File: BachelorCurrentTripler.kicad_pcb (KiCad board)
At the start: 2 copper layers, 54 parts, among them Q13 C2M0025120D, Q14 C2M0025120D, Q15 C2M0025120D, Q16 C2M0025120D, Q7 C2M0025120D, Q8 C2M0025120D, U1 STDriveG600, U2 STDriveG600, U3 STDriveG600

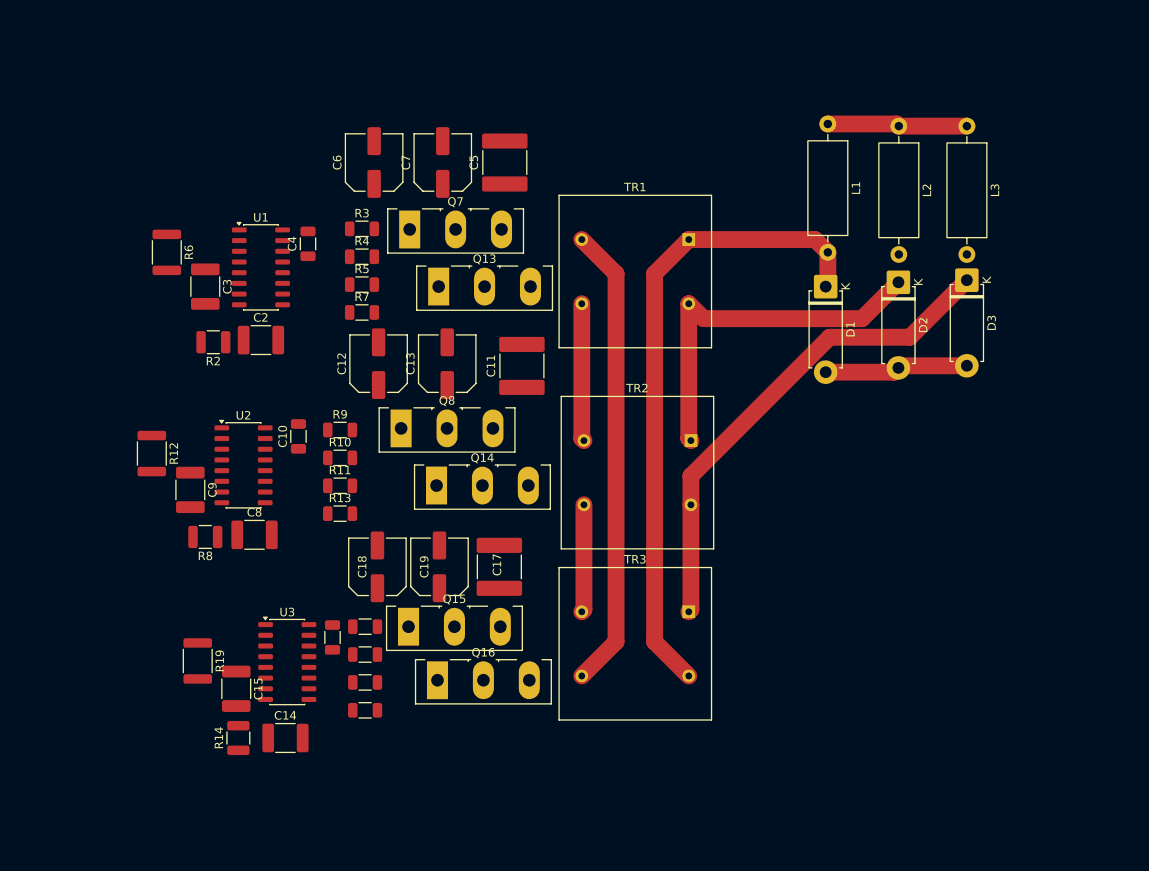
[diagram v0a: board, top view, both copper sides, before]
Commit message: added a board outline and some holes
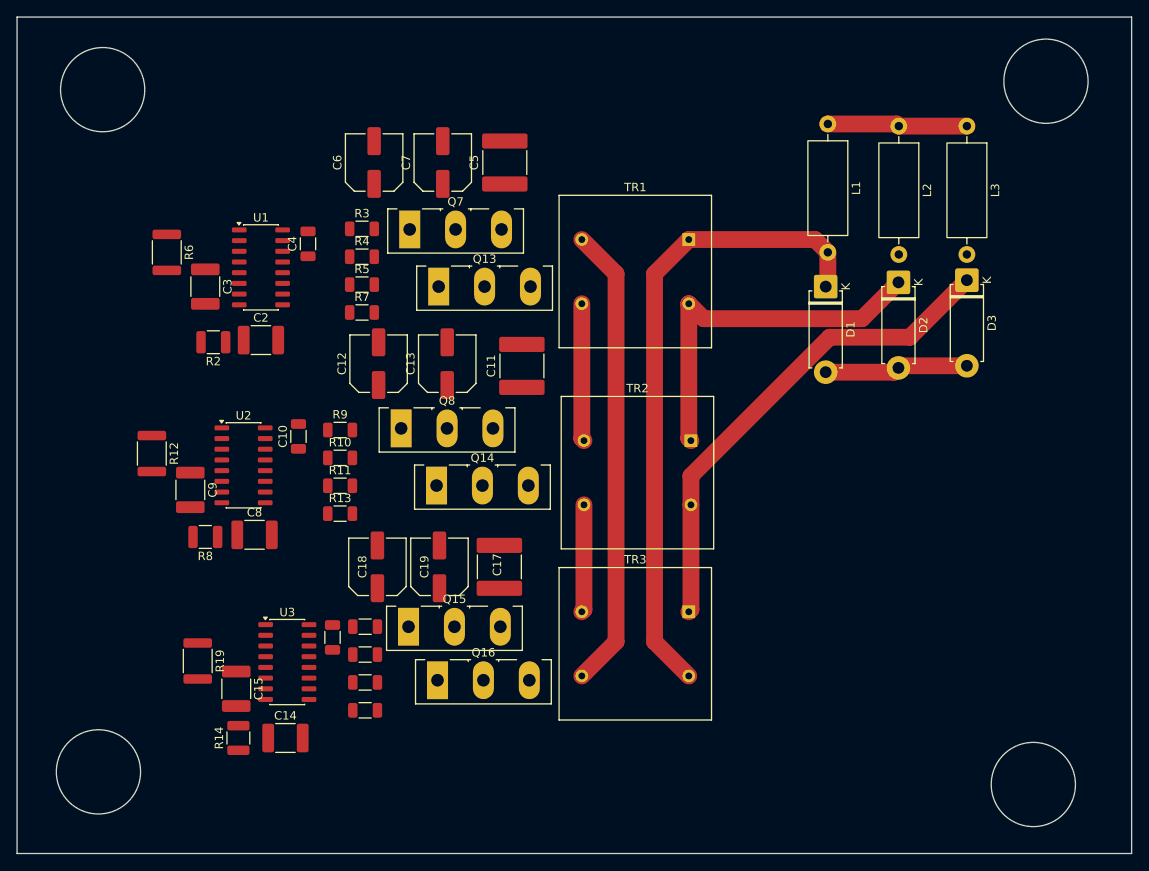
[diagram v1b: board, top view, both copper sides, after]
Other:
- board outline added: 132.3 x 99.3 mm
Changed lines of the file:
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@@
 		)
+	)
+	(gr_circle
+		(center 207 63.5)
+		(end 212 63.5)
+		(stroke
+			(width 0.05)
+			(type default)
+		)
+		(fill no)
+		(layer "Edge.Cuts")
+	)
+	(gr_circle
+		(center 94.5 145.5)
+		(end 99.5 145.5)
+		(stroke
+			(width 0.05)
+			(type default)
+		)
+		(fill no)
+		(layer "Edge.Cuts")
+	)
+	(gr_rect
+		(start 84.836 55.88)
+		(end 217.17 155.194)
+		(stroke
+			(width 0.05)
+			(type default)
+		)
+		(fill no)
+		(layer "Edge.Cuts")
+	)
+	(gr_circle
+		(center 205.5 147)
+		(end 210.5 147)
+		(stroke
+			(width 0.05)
+			(type default)
+		)
+		(fill no)
+		(layer "Edge.Cuts")
+	)
+	(gr_circle
+		(center 95 64.5)
+		(end 100 64.5)
+		(stroke
+			(width 0.05)
+			(type default)
+		)
+		(fill no)
+		(layer "Edge.Cuts")
 	)
 	(segment

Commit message: intial pcb layout
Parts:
- removed D1, D2, D3: D, Diode_THT:D_5W_P10.16mm_Horizontal
- removed L1, L2, L3: L, Inductor_THT:L_Axial_L11.0mm_D4.5mm_P15.24mm_Horizontal_Fastron_MECC
- removed TR1, TR2, TR3: 48:2, Transformer_THT:Transformer_NF_ETAL_1-1_P1200
- added J1: Conn_01x07_Pin, Connector_JST:JST_EH_B7B-EH-A_1x07_P2.50mm_Vertical, F.Cu at (90.8, 107.5)
- added J2: Conn_01x01_Pin, Connector_Wire:SolderWirePad_1x01_SMD_5x10mm, F.Cu at (91.0, 75.9)
- added J3: Conn_01x01_Pin, Connector_Wire:SolderWirePad_1x01_SMD_5x10mm, F.Cu at (91.0, 85.0)
- added J4: Conn_01x04_Socket, Connector_Hirose:Hirose_DF63M-4P-3.96DSA_1x04_P3.96mm_Vertical, F.Cu at (158.5, 97.1)
- added J5: Conn_01x01_Pin, Connector_Wire:SolderWirePad_1x01_SMD_5x10mm, F.Cu at (91.0, 94.5)
- Q13, Q14, Q15, Q16, Q7, Q8: footprint Package_TO_SOT_THT:TO-247-3_Vertical -> Package_TO_SOT_SMD:TO-252-2
- moved C17 18.3 mm to (146.0, 139.0), turned to -90 degrees
- moved C11 16.3 mm to (149.0, 113.0), turned to -90 degrees
- moved C19 13.8 mm to (147.0, 128.0)
- moved C13 13.3 mm to (149.0, 99.5)
- moved U2 12.8 mm to (124.4, 107.7)
- moved C12 11.7 mm to (139.5, 97.5)
- moved Q8 10.4 mm to (140.8, 105.6)
- moved Q13 8.76 mm to (143.5, 89.3)
- moved C10 8.63 mm to (125.5, 101.0), turned to 0 degrees
- moved R10 8.53 mm to (131.5, 106.3)
- moved R11 8.53 mm to (131.5, 109.6)
- moved R13 8.53 mm to (131.5, 112.9)
- moved R9 8.53 mm to (131.5, 103.0)
- moved Q7 8.51 mm to (139.9, 82.0)
- moved C18 7.44 mm to (134.5, 124.0), turned to 180 degrees
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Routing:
- net +48V: track 0.00 -> 128.9 mm, vias 0 -> 20
- net +12V: track 0.00 -> 80.6 mm, vias 0 -> 20
- net /Transformer/SecondaryA: track 76.5 -> 0.00 mm
- net /Transformer/SecondaryC: track 58.6 -> 0.00 mm
- net /PhaseC/COUT: track 12.8 -> 68.4 mm
- net /PhaseA/AOUT: track 55.2 -> 0.00 mm
- net /Transformer/SecondaryB: track 43.8 -> 0.00 mm
- net +1V2: track 16.6 -> 0.00 mm
- net /PhaseB/BOUT: track 16.4 -> 0.00 mm
- net /PhaseC/PVCC: track 0.00 -> 12.2 mm
- net Net-(U3-SD): track 0.00 -> 10.4 mm
- net Net-(Q15-G): track 0.00 -> 7.16 mm
- net Net-(Q16-G): track 0.00 -> 6.04 mm
- net GND: track 17.1 -> 22.4 mm, vias 0 -> 32
- net Net-(U3-LOFF): track 0.00 -> 3.26 mm
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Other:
- board size 132.3 x 99.3 mm -> 81.8 x 81.3 mm
- copper layers 2 -> 4
- board text added: "10-15V max"
- board text added: "48V max"
- board text added: "GND"
- board text added: "J2"

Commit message: added more to the layout
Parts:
- moved C5 17.0 mm to (148.3, 89.2), turned to -90 degrees
- moved C7 15.8 mm to (149.4, 80.5), turned to 0 degrees
- moved C9 14.3 mm to (119.6, 110.2)
- moved R12 14.3 mm to (115.1, 106.7)
- moved C6 14.0 mm to (141.2, 73.7)
- moved C8 12.6 mm to (125.5, 115.6)
- moved R8 12.5 mm to (119.6, 116.3)
- moved C2 11.9 mm to (125.5, 91.9)
- moved R2 11.8 mm to (119.6, 91.7)
- moved C3 11.6 mm to (118.6, 86.1)
- moved U1 10.9 mm to (124.7, 84.7)
- moved C4 7.88 mm to (126.0, 78.5), turned to 0 degrees
- moved R6 7.35 mm to (114.6, 84.1)
- moved R4 5.62 mm to (130.8, 81.8)
- moved R3 5.32 mm to (130.8, 79.2)
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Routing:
- net +12V: track 80.6 -> 148.1 mm
- net +48V: track 128.9 -> 191.2 mm, vias 20 -> 44
- net /PhaseA/ALin: track 0.00 -> 45.2 mm
- net /PhaseA/AHin: track 0.00 -> 44.1 mm
- net /PhaseC/COUT: track 68.4 -> 26.8 mm
- net /PhaseB/BLIN: track 0.00 -> 36.0 mm
- net /PhaseB/BHIN: track 0.00 -> 36.0 mm
- net /PhaseC/CHIN: track 1.26 -> 34.9 mm
- net /PhaseC/CLIN: track 0.00 -> 33.6 mm
- net /PhaseB/PVCC: track 0.00 -> 10.3 mm
- net /PhaseA/PVCC: track 0.00 -> 10.1 mm
- net Net-(U2-SD): track 0.00 -> 8.21 mm
- net Net-(U1-SD): track 0.00 -> 7.72 mm
- net GND: track 22.4 -> 26.0 mm, vias 32 -> 97
- net Net-(U3-BOOT): track 2.24 -> 0.00 mm
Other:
- outline, holes or cut-outs redrawn

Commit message: board should be done now
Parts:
- moved R14 2.13 mm to (117.5, 138.0), turned to 180 degrees
- moved R4 0.74 mm to (131.0, 82.5)
- moved R3 0.74 mm to (131.0, 80.0)
- moved C17 0.50 mm to (147.2, 135.3)
- moved C19 0.50 mm to (148.2, 124.3)
- moved R16 0.50 mm to (129.2, 128.3)
- moved C18 0.50 mm to (135.7, 120.3)
- moved R15 0.50 mm to (129.2, 125.8)
- moved C14 0.50 mm to (122.7, 138.3)
- moved C15 0.50 mm to (115.7, 131.3)
- moved Q15 0.50 mm to (138.7, 128.0)
- moved Q16 0.50 mm to (138.7, 135.1)
- moved R17 0.50 mm to (129.7, 132.8)
- moved R18 0.50 mm to (129.7, 135.3)
- moved R19 0.50 mm to (110.2, 129.3)
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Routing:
- net /PhaseB/BOUT: track 0.00 -> 46.7 mm
- net /PhaseC/COUT: track 26.8 -> 69.0 mm
- net /PhaseA/AOUT: track 0.00 -> 39.5 mm
- net +12V: track 148.1 -> 180.5 mm, vias 20 -> 29
- net +48V: track 191.2 -> 208.7 mm, vias 44 -> 70
- net GND: track 26.0 -> 42.7 mm, vias 97 -> 109
- net Net-(Q13-G): track 0.00 -> 6.26 mm
- net Net-(Q7-G): track 0.00 -> 6.26 mm
- net Net-(Q8-G): track 0.00 -> 6.00 mm
- net Net-(Q14-G): track 0.00 -> 5.51 mm
- net Net-(U1-LOFF): track 0.00 -> 3.16 mm
- net Net-(U1-HON): track 0.00 -> 2.94 mm
- net Net-(U2-LOFF): track 0.00 -> 2.92 mm
- net Net-(U2-HON): track 0.00 -> 2.79 mm
- net Net-(U2-LON): track 0.00 -> 2.45 mm
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- added copper zone on In1.Cu, net GND
